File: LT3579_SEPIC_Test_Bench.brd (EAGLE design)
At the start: 74 x 58 mm, 159 parts

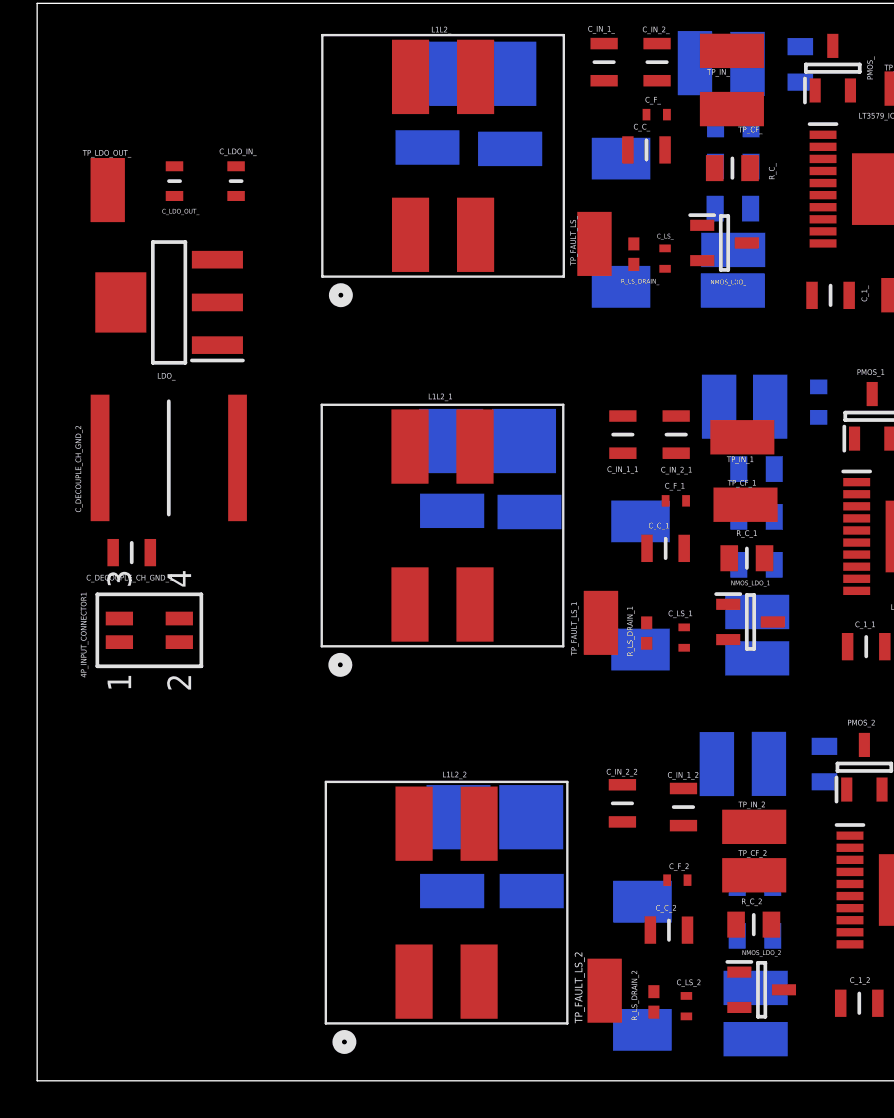
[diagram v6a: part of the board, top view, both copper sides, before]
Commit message: Added Reverse Voltage Protection PMOS
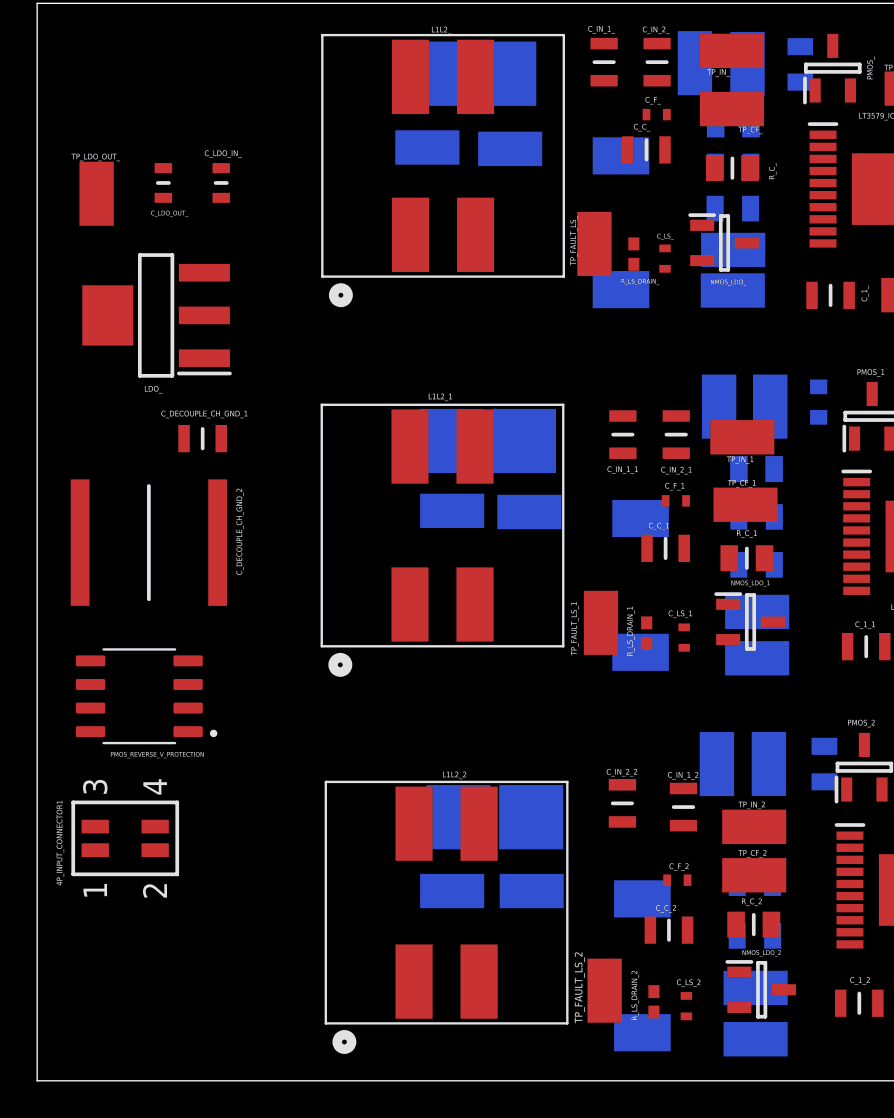
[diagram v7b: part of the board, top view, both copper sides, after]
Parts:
- added PMOS_REVERSE_V_PROTECTION: DMP3015LSSQ-13, DMP3015LSSQ-13:SOIC127P600X170-8N
- D1_, D1_1, D1_2: value MBRS360T3G -> MBRS330T3G; device SamacSys_Parts:DIOM8059X261N -> SamacSys_Parts:DIOM7958X256N
- R_GATE_, R_GATE_1, R_GATE_2: value AC0805DR-0710KL -> AC0805FR-0710KL; device AC0805DR-0710KL:RESC2012X60N -> SamacSys_Parts:RESC2012X60N
- moved 4P_INPUT_CONNECTOR1 11.3 mm to (4.74, 13.1)
- moved C_DECOUPLE_CH_GND_1 7.23 mm to (8.91, 34.6), turned to 0 degrees
- moved C_DECOUPLE_CH_GND_2 4.68 mm to (6.01, 29.0), turned to 0 degrees
- moved LDO_ 0.99 mm to (6.40, 41.2)
- moved C_LDO_IN_ 0.81 mm to (9.91, 48.3)
- moved TP_LDO_OUT_ 0.63 mm to (3.20, 47.8)
- moved C_LDO_OUT_ 0.61 mm to (6.79, 48.3)
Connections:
- new net VIN_CONNECTOR: 4P_INPUT_CONNECTOR1.1, 4P_INPUT_CONNECTOR1.3, PMOS_REVERSE_V_PROTECTION.5, PMOS_REVERSE_V_PROTECTION.6, PMOS_REVERSE_V_PROTECTION.7, PMOS_REVERSE_V_PROTECTION.8
- net 0: now also PMOS_REVERSE_V_PROTECTION.4
- net VIN: now also PMOS_REVERSE_V_PROTECTION.1, PMOS_REVERSE_V_PROTECTION.2, PMOS_REVERSE_V_PROTECTION.3; no longer 4P_INPUT_CONNECTOR1.1, 4P_INPUT_CONNECTOR1.3

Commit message: Modified Board
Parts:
- moved R_SHUNT_GND_2 0.36 mm to (24.4, 14.4), turned to 180 degrees
- moved R_SHUNT_GND_1 0.23 mm to (24.4, 34.6), turned to 180 degrees
- moved PMOS_REVERSE_V_PROTECTION 0.18 mm to (5.32, 20.7)
- moved 4P_INPUT_CONNECTOR1 0.07 mm to (4.67, 13.1)
